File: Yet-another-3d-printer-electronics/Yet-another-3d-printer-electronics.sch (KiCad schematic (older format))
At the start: 28 parts, among them CON1 SD_Card, J1 LCD_Connector, P19 END2_TEMP, P2 BEDTEMP, P3 END1_TEMP, SW1 Switch_DPST, U2 LPC1114FBD48/302, X1 CRYSTAL_SMD

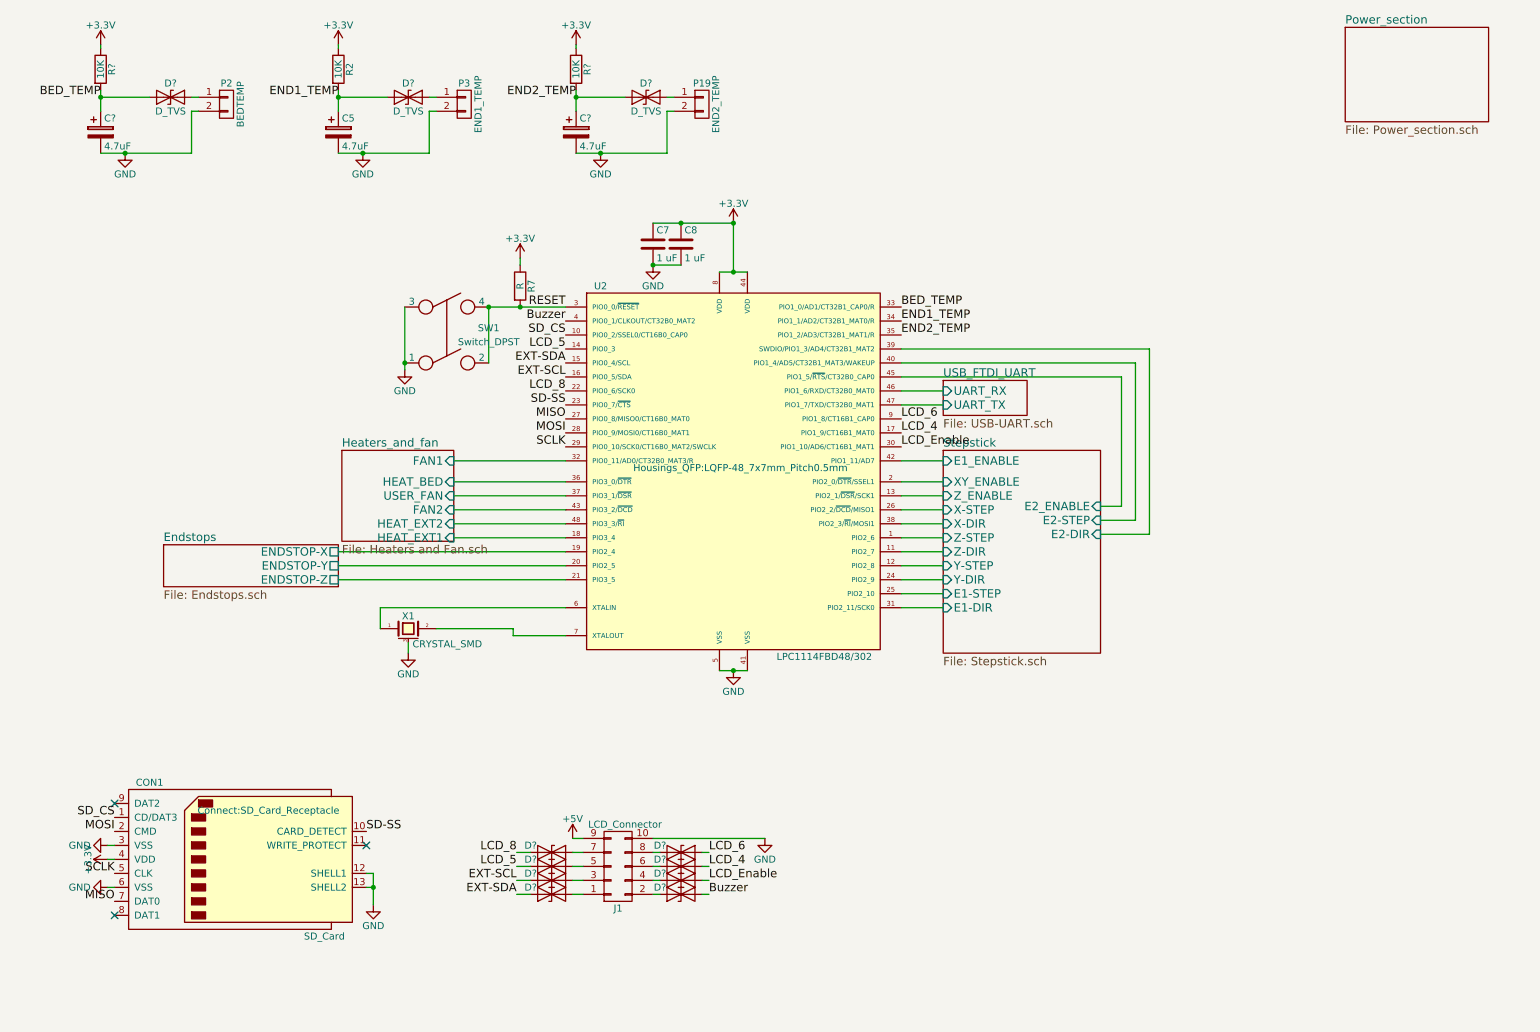
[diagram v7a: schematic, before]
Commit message: Add programming jumper
Signed-off-by: Mateusz Krawczuk <mat.krawczuk@gmail.com>
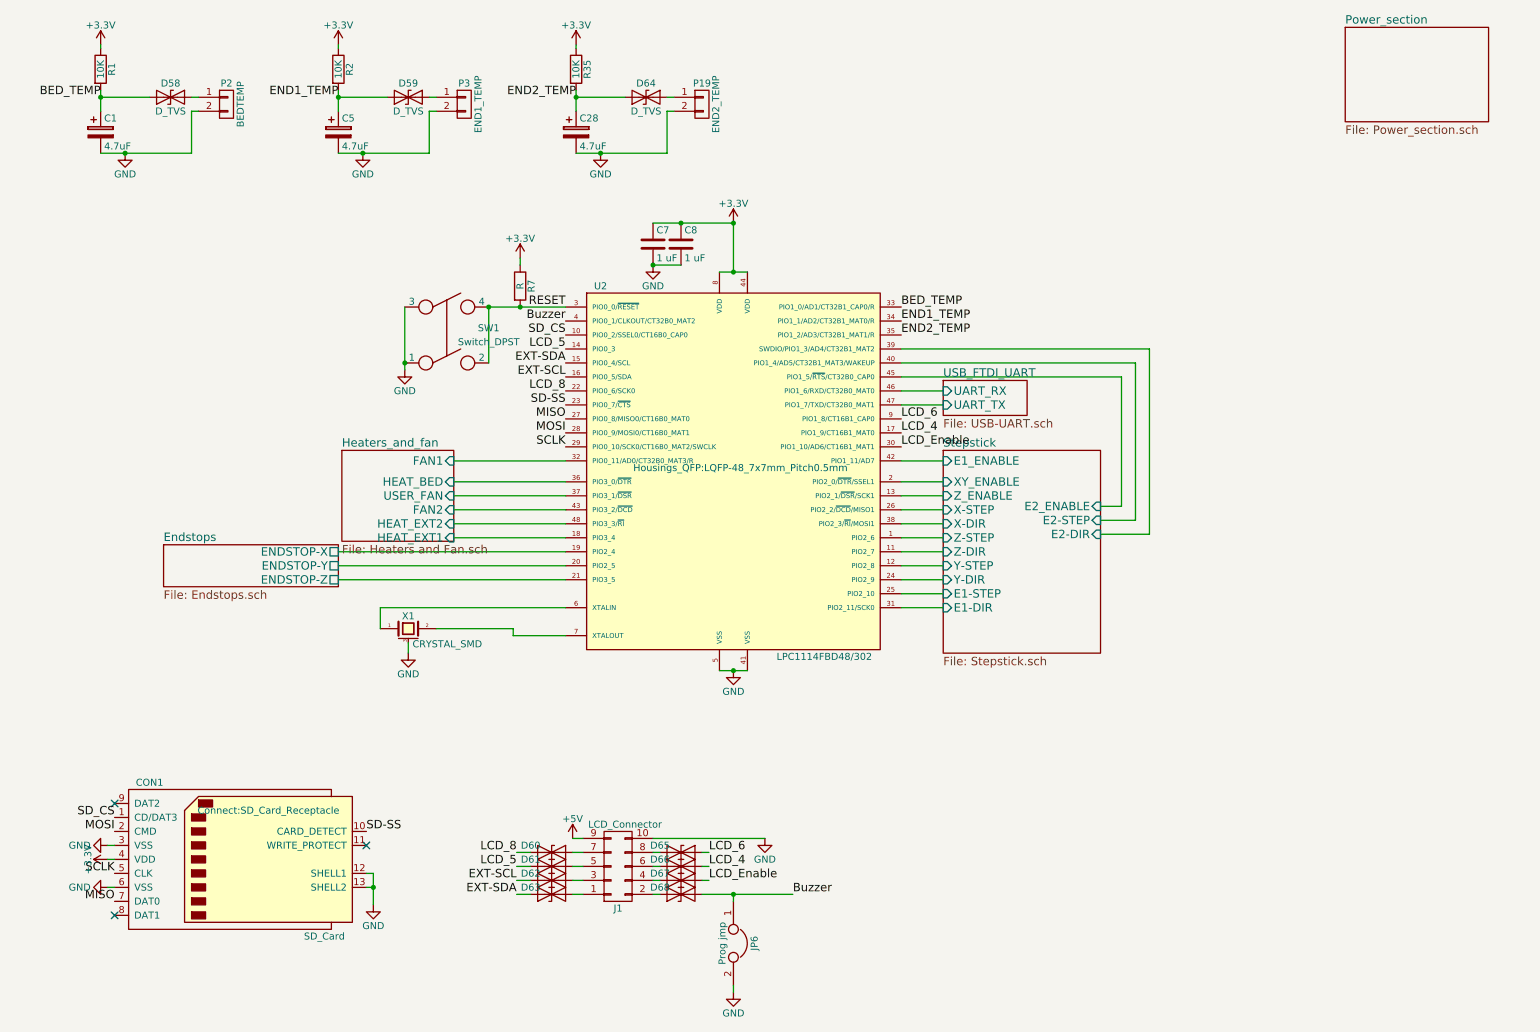
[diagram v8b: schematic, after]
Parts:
- added JP6: Prog jmp, symbol Jumper
- gave numbers to parts that had none: 15
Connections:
- net Buzzer: now also JP6.1
- net GND: now also JP6.2
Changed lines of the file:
@@
 RESET
 $Comp
-L GND #PWR01
+L GND #PWR17
 U 1 1 588666E7
 P 5675 5225
-F 0 "#PWR01" H 5675 4975 50  0001 C CNN
+F 0 "#PWR17" H 5675 4975 50  0001 C CNN
 F 1 "GND" H 5675 5075 50  0000 C CNN
 F 2 "" H 5675 5225 50  0000 C CNN
@@
 $EndComp
 $Comp
-L GND #PWR02
+L GND #PWR15
 U 1 1 5883A250
 P 5100 2325
-F 0 "#PWR02" H 5100 2075 50  0001 C CNN
+F 0 "#PWR15" H 5100 2075 50  0001 C CNN
 F 1 "GND" H 5100 2175 50  0000 C CNN
 F 2 "" H 5100 2325 50  0000 C CNN
@@
 $EndComp
 $Comp
-L GND #PWR03
+L GND #PWR10
 U 1 1 58852DAD
 P 3350 5100
-F 0 "#PWR03" H 3350 4850 50  0001 C CNN
+F 0 "#PWR10" H 3350 4850 50  0001 C CNN
 F 1 "GND" H 3350 4950 50  0000 C CNN
 F 2 "" H 3350 5100 50  0000 C CNN
@@
 $EndComp
 $Comp
-L GND #PWR04
+L GND #PWR9
 U 1 1 58868622
 P 3325 3075
-F 0 "#PWR04" H 3325 2825 50  0001 C CNN
+F 0 "#PWR9" H 3325 2825 50  0001 C CNN
 F 1 "GND" H 3325 2925 50  0000 C CNN
 F 2 "" H 3325 3075 50  0000 C CNN
@@
 NoConn ~ 3050 6475
 $Comp
-L GND #PWR07
+L GND #PWR8
 U 1 1 588EF0E4
 P 3100 6900
-F 0 "#PWR07" H 3100 6650 50  0001 C CNN
+F 0 "#PWR8" H 3100 6650 50  0001 C CNN
 F 1 "GND" H 3100 6750 50  0000 C CNN
 F 2 "" H 3100 6900 50  0000 C CNN
@@
 $EndComp
 $Comp
-L GND #PWR08
+L GND #PWR2
 U 1 1 5890B49A
 P 1200 6475
-F 0 "#PWR08" H 1200 6225 50  0001 C CNN
+F 0 "#PWR2" H 1200 6225 50  0001 C CNN
 F 1 "GND" V 1200 6275 50  0000 C CNN
 F 2 "" H 1200 6475 50  0000 C CNN
@@
 SD-SS
 $Comp
-L GND #PWR09
+L GND #PWR4
 U 1 1 5890D76C
 P 1200 6775
-F 0 "#PWR09" H 1200 6525 50  0001 C CNN
+F 0 "#PWR4" H 1200 6525 50  0001 C CNN
 F 1 "GND" V 1200 6575 50  0000 C CNN
 F 2 "" H 1200 6775 50  0000 C CNN
@@
 $EndSheet
 $Comp
-L +3.3V #PWR010
+L +3.3V #PWR16
 U 1 1 58FDAA0A
 P 5675 2025
-F 0 "#PWR010" H 5675 1875 50  0001 C CNN
+F 0 "#PWR16" H 5675 1875 50  0001 C CNN
 F 1 "+3.3V" H 5675 2165 50  0000 C CNN
 F 2 "" H 5675 2025 50  0001 C CNN
@@
 Connection ~ 5675 2025
 $Comp
-L +3.3V #PWR011
+L +3.3V #PWR11
 U 1 1 58FDADD2
 P 4150 2275
-F 0 "#PWR011" H 4150 2125 50  0001 C CNN
+F 0 "#PWR11" H 4150 2125 50  0001 C CNN
 F 1 "+3.3V" H 4150 2415 50  0000 C CNN
 F 2 "" H 4150 2275 50  0001 C CNN
@@
 	2850 4375 4475 4375
 $Comp
-L +5V #PWR012
+L +5V #PWR12
 U 1 1 58FE5EAC
 P 4525 6425
-F 0 "#PWR012" H 4525 6275 50  0001 C CNN
+F 0 "#PWR12" H 4525 6275 50  0001 C CNN
 F 1 "+5V" H 4525 6565 50  0000 C CNN
 F 2 "" H 4525 6425 50  0001 C CNN
@@
 $EndComp
 $Comp
-L GND #PWR013
+L GND #PWR19
 U 1 1 58FE5F48
 P 5900 6425
-F 0 "#PWR013" H 5900 6175 50  0001 C CNN
+F 0 "#PWR19" H 5900 6175 50  0001 C CNN
 F 1 "GND" H 5900 6275 50  0000 C CNN
 F 2 "" H 5900 6425 50  0001 C CNN
@@
 	1    0    0    -1
 $EndComp
-Text Label 5500 6825 0    60   ~ 0
+Text Label 6100 6825 0    60   ~ 0
 Buzzer
 Text Label 5500 6725 0    60   ~ 0
@@
 	4475 4175 3675 4175
 $Comp
-L +3.3V #PWR016
+L +3.3V #PWR3
 U 1 1 5900DC8E
 P 1200 6575
-F 0 "#PWR016" H 1200 6425 50  0001 C CNN
+F 0 "#PWR3" H 1200 6425 50  0001 C CNN
 F 1 "+3.3V" H 1200 6715 50  0000 C CNN
 F 2 "" H 1200 6575 50  0001 C CNN
@@
 	7175 3725 6875 3725
 $Comp
-L D_TVS D?
+L D_TVS D65
 U 1 1 59048B79
 P 5300 6525
-F 0 "D?" H 5150 6575 50  0000 C CNN
+F 0 "D65" H 5150 6575 50  0000 C CNN
 F 1 "D_TVS" H 5300 6425 50  0001 C CNN
 F 2 "" H 5300 6525 50  0001 C CNN
@@
 	5500 6525 5450 6525
 $Comp
-L D_TVS D?
+L D_TVS D66
 U 1 1 5904956A
 P 5300 6625
-F 0 "D?" H 5150 6675 50  0000 C CNN
+F 0 "D66" H 5150 6675 50  0000 C CNN
 F 1 "D_TVS" H 5300 6525 50  0001 C CNN
 F 2 "" H 5300 6625 50  0001 C CNN
@@
 $EndComp
 $Comp
-L D_TVS D?
+L D_TVS D67
 U 1 1 5904964D
 P 5300 6725
-F 0 "D?" H 5150 6775 50  0000 C CNN
+F 0 "D67" H 5150 6775 50  0000 C CNN
 F 1 "D_TVS" H 5300 6625 50  0001 C CNN
 F 2 "" H 5300 6725 50  0001 C CNN
@@
 $EndComp
 $Comp
-L D_TVS D?
+L D_TVS D68
 U 1 1 59049737
 P 5300 6825
-F 0 "D?" H 5150 6875 50  0000 C CNN
+F 0 "D68" H 5150 6875 50  0000 C CNN
 F 1 "D_TVS" H 5100 6725 50  0001 C CNN
 F 2 "" H 5300 6825 50  0001 C CNN
@@
 $EndComp
 Wire Wire Line
-	5500 6825 5450 6825
+	5450 6825 6100 6825
 Wire Wire Line
 	5450 6725 5500 6725
@@
 	5500 6625 5450 6625
 $Comp
-L D_TVS D?
+L D_TVS D60
 U 1 1 5904A740
 P 4375 6525
-F 0 "D?" H 4225 6575 50  0000 C CNN
+F 0 "D60" H 4225 6575 50  0000 C CNN
 F 1 "D_TVS" H 4375 6425 50  0001 C CNN
 F 2 "" H 4375 6525 50  0001 C CNN
@@
 $EndComp
 $Comp
-L D_TVS D?
+L D_TVS D61
 U 1 1 5904A746
 P 4375 6625
-F 0 "D?" H 4225 6675 50  0000 C CNN
+F 0 "D61" H 4225 6675 50  0000 C CNN
 F 1 "D_TVS" H 4375 6525 50  0001 C CNN
 F 2 "" H 4375 6625 50  0001 C CNN
@@
 $EndComp
 $Comp
-L D_TVS D?
+L D_TVS D62
 U 1 1 5904A74C
 P 4375 6725
-F 0 "D?" H 4225 6775 50  0000 C CNN
+F 0 "D62" H 4225 6775 50  0000 C CNN
 F 1 "D_TVS" H 4375 6625 50  0001 C CNN
 F 2 "" H 4375 6725 50  0001 C CNN
@@
 $EndComp
 $Comp
-L D_TVS D?
+L D_TVS D63
 U 1 1 5904A752
 P 4375 6825
-F 0 "D?" H 4225 6875 50  0000 C CNN
+F 0 "D63" H 4225 6875 50  0000 C CNN
 F 1 "D_TVS" H 4175 6725 50  0001 C CNN
 F 2 "" H 4375 6825 50  0001 C CNN
@@
 $EndComp
 $Comp
-L +3.3V #PWR014
+L +3.3V #PWR6
 U 1 1 5900830A
 P 2850 750
-F 0 "#PWR014" H 2850 600 50  0001 C CNN
+F 0 "#PWR6" H 2850 600 50  0001 C CNN
 F 1 "+3.3V" H 2850 890 50  0000 C CNN
 F 2 "" H 2850 750 50  0001 C CNN
@@
 END1_TEMP
 $Comp
-L GND #PWR06
+L GND #PWR7
 U 1 1 588E3505
 P 3025 1525
-F 0 "#PWR06" H 3025 1275 50  0001 C CNN
+F 0 "#PWR7" H 3025 1275 50  0001 C CNN
 F 1 "GND" H 3025 1375 50  0000 C CNN
 F 2 "" H 3025 1525 50  0000 C CNN
@@
 $EndComp
 $Comp
-L D_TVS D?
+L D_TVS D59
 U 1 1 590523B4
 P 3350 1125
-F 0 "D?" H 3350 1225 50  0000 C CNN
+F 0 "D59" H 3350 1225 50  0000 C CNN
 F 1 "D_TVS" H 3350 1025 50  0000 C CNN
 F 2 "" H 3350 1125 50  0001 C CNN
@@
 $EndComp
 $Comp
-L +3.3V #PWR?
+L +3.3V #PWR1
 U 1 1 59052ED6
 P 1150 750
-F 0 "#PWR?" H 1150 600 50  0001 C CNN
+F 0 "#PWR1" H 1150 600 50  0001 C CNN
 F 1 "+3.3V" H 1150 890 50  0000 C CNN
 F 2 "" H 1150 750 50  0001 C CNN
@@
 Connection ~ 1150 1125
 $Comp
-L GND #PWR?
+L GND #PWR5
 U 1 1 59052EE3
 P 1325 1525
-F 0 "#PWR?" H 1325 1275 50  0001 C CNN
+F 0 "#PWR5" H 1325 1275 50  0001 C CNN
 F 1 "GND" H 1325 1375 50  0000 C CNN
 F 2 "" H 1325 1525 50  0000 C CNN
@@
 $EndComp
 $Comp
-L CP C?
+L CP C1
 U 1 1 59052EE9
 P 1150 1375
-F 0 "C?" H 1175 1475 50  0000 L CNN
+F 0 "C1" H 1175 1475 50  0000 L CNN
 F 1 "4.7uF" H 1175 1275 50  0000 L CNN
 F 2 "Capacitors_ThroughHole:CP_Radial_D4.0mm_P2.00mm" H 1188 1225 50  0001 C CNN
@@
 $EndComp
 $Comp
-L R R?
+L R R1
 U 1 1 59052EEF
 P 1150 925
-F 0 "R?" V 1230 925 50  0000 C CNN
+F 0 "R1" V 1230 925 50  0000 C CNN
 F 1 "10K" V 1150 925 50  0000 C CNN
 F 2 "Resistors_SMD:R_0805_HandSoldering" V 1080 925 50  0001 C CNN
@@
 $EndComp
 $Comp
-L D_TVS D?
+L D_TVS D58
 U 1 1 59052EFB
 P 1650 1125
-F 0 "D?" H 1650 1225 50  0000 C CNN
+F 0 "D58" H 1650 1225 50  0000 C CNN
 F 1 "D_TVS" H 1650 1025 50  0000 C CNN
 F 2 "" H 1650 1125 50  0001 C CNN
@@
 	1800 1225 1800 1525
 $Comp
-L +3.3V #PWR?
+L +3.3V #PWR13
 U 1 1 59054E63
 P 4550 750
-F 0 "#PWR?" H 4550 600 50  0001 C CNN
+F 0 "#PWR13" H 4550 600 50  0001 C CNN
 F 1 "+3.3V" H 4550 890 50  0000 C CNN
 F 2 "" H 4550 750 50  0001 C CNN
@@
 Connection ~ 4550 1125
 $Comp
-L GND #PWR?
+L GND #PWR14
 U 1 1 59054E70
 P 4725 1525
-F 0 "#PWR?" H 4725 1275 50  0001 C CNN
+F 0 "#PWR14" H 4725 1275 50  0001 C CNN
 F 1 "GND" H 4725 1375 50  0000 C CNN
 F 2 "" H 4725 1525 50  0000 C CNN
@@
 $EndComp
 $Comp
-L CP C?
+L CP C28
 U 1 1 59054E76
 P 4550 1375
-F 0 "C?" H 4575 1475 50  0000 L CNN
+F 0 "C28" H 4575 1475 50  0000 L CNN
 F 1 "4.7uF" H 4575 1275 50  0000 L CNN
 F 2 "Capacitors_ThroughHole:CP_Radial_D4.0mm_P2.00mm" H 4588 1225 50  0001 C CNN
@@
 $EndComp
 $Comp
-L R R?
+L R R35
 U 1 1 59054E7C
 P 4550 925
-F 0 "R?" V 4630 925 50  0000 C CNN
+F 0 "R35" V 4630 925 50  0000 C CNN
 F 1 "10K" V 4550 925 50  0000 C CNN
 F 2 "Resistors_SMD:R_0805_HandSoldering" V 4480 925 50  0001 C CNN
@@
 $EndComp
 $Comp
-L D_TVS D?
+L D_TVS D64
 U 1 1 59054E88
 P 5050 1125
-F 0 "D?" H 5050 1225 50  0000 C CNN
+F 0 "D64" H 5050 1225 50  0000 C CNN
 F 1 "D_TVS" H 5050 1025 50  0000 C CNN
 F 2 "" H 5050 1125 50  0001 C CNN
@@
 Wire Wire Line
 	5200 1225 5200 1525
+Connection ~ 5675 6825
+$Comp
+L Jumper JP6
+U 1 1 5905FADD
+P 5675 7175
+F 0 "JP6" H 5675 7325 50  0000 C CNN
+F 1 "Prog jmp" H 5675 7095 50  0000 C CNN
+F 2 "" H 5675 7175 50  0001 C CNN
+F 3 "" H 5675 7175 50  0001 C CNN
+	1    5675 7175
+	0    1    1    0
+$EndComp
+$Comp
+L GND #PWR18
+U 1 1 5905FBE0
+P 5675 7525
+F 0 "#PWR18" H 5675 7275 50  0001 C CNN
+F 1 "GND" H 5675 7375 50  0000 C CNN
+F 2 "" H 5675 7525 50  0001 C CNN
+F 3 "" H 5675 7525 50  0001 C CNN
+	1    5675 7525
+	1    0    0    -1
+$EndComp
+Wire Wire Line
+	5675 7525 5675 7475
+Wire Wire Line
+	5675 6825 5675 6875
 $EndSCHEMATC
